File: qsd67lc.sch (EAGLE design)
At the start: 21 parts, among them IC1 MEGA8-P

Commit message: changed supply from 5V to 3V3
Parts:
- added JP1, JP2, JP3: (no value), pinhead:PINHD-1X3
- added U1: HC_05, Bluetooth HC-05:HC_05
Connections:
- net RXD_5V renamed RXD
- net TXD_5V renamed TXD
- removed net +5V: IC1.AREF, IC1.AVCC, IC1.VCC@1, R1.2, SV1.5
- removed net DLE: R2.2, R3.2, R4.2, R5.2, R6.2
- new net +3V3: IC1.AREF, IC1.AVCC, IC1.VCC@1, R1.2, R2.2, R3.2, R4.2, R5.2, R6.2
- new net MISO_EXT: JP2.1
- new net MISO_ISP: JP2.3, SV1.6
- new net MOSI_EXT: JP1.1
- new net MOSI_ISP: JP1.3, SV1.3
- new net SCK_EXT: JP3.1
- new net SCK_ISP: JP3.3, SV1.4
- net MISO: now also JP2.2; no longer SV1.6
- net MOSI: now also JP1.2; no longer SV1.3
- net SCK: now also JP3.2; no longer SV1.4
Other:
- note added: "jumper to detach other SPI devices while programming"

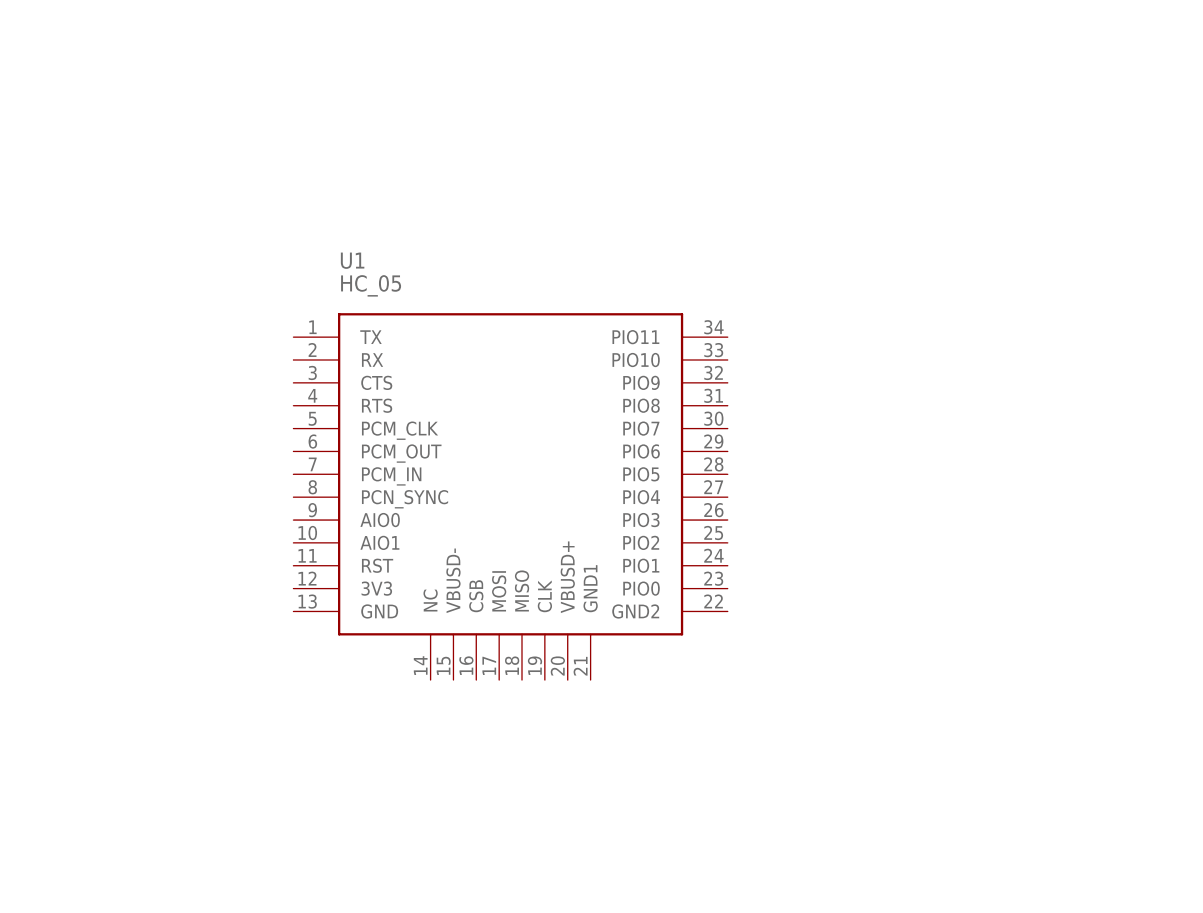
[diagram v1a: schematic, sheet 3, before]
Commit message: added hc05 circuits
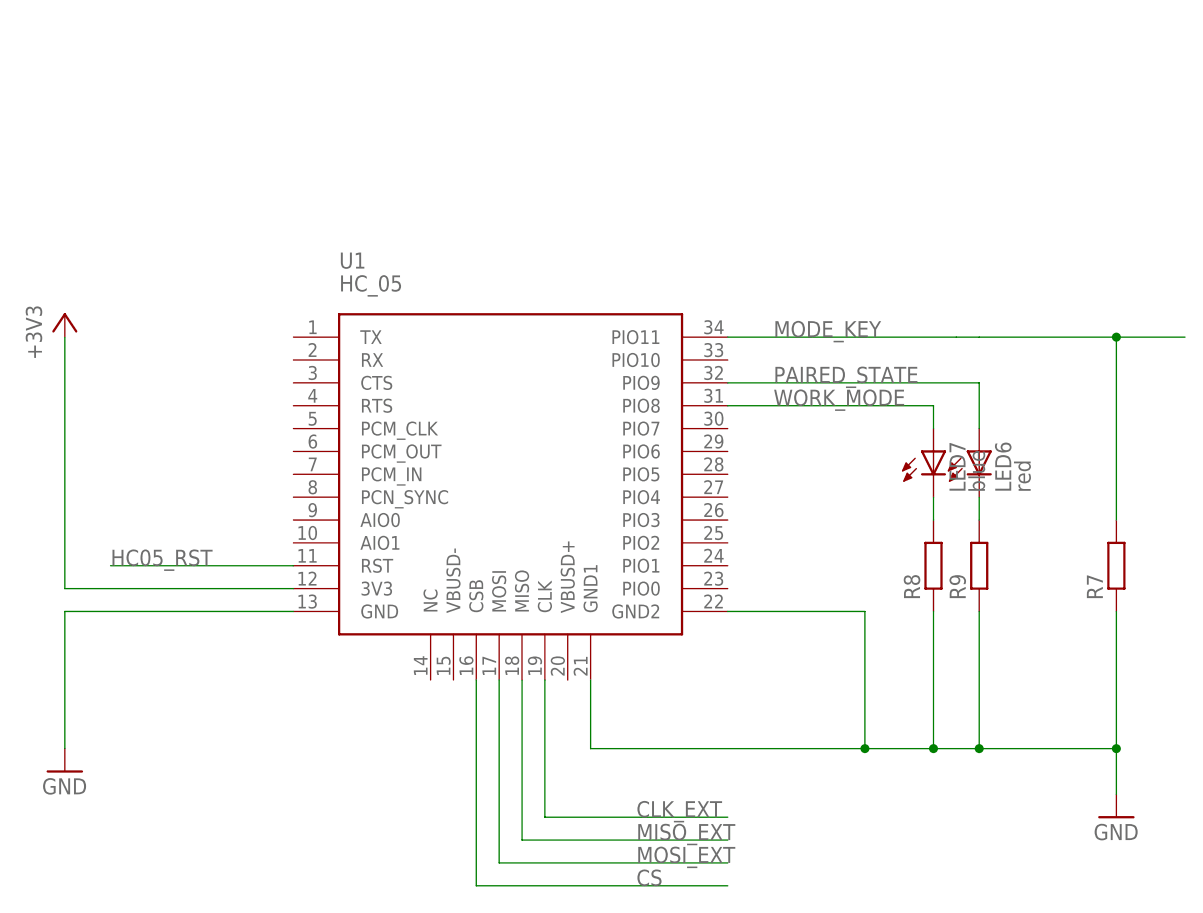
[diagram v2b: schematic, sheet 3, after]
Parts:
- added LED6: red, led:LEDCHIP-LED0805
- added LED7: blue, led:LEDCHIP-LED0805
- added R7, R8, R9: (no value), rcl:R-EU_R0805
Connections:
- new net CLK_EXT: U1.CLK
- new net CS: IC1.PB2(SS/OC1B), U1.CSB
- new net HC05_RST: IC1.PB0(ICP), U1.RST
- new net MODE_KEY: R7.2, U1.PIO11
- new net N$13: LED7.C, R8.2
- new net N$14: LED6.C, R9.2
- new net PAIRED_STATE: LED6.A, U1.PIO9
- new net WORK_MODE: LED7.A, U1.PIO8
- net +3V3: now also U1.3V3
- net GND: now also R7.1, R8.1, R9.1, U1.GND, U1.GND1, U1.GND2
- net MISO_EXT: now also U1.MISO
- net MOSI_EXT: now also U1.MOSI
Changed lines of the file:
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@@
 <part name="JP2" library="pinhead" library_urn="urn:adsk.eagle:library:325" deviceset="PINHD-1X3" device="" package3d_urn="urn:adsk.eagle:package:22458/2"/>
 <part name="JP3" library="pinhead" library_urn="urn:adsk.eagle:library:325" deviceset="PINHD-1X3" device="" package3d_urn="urn:adsk.eagle:package:22458/2"/>
+<part name="+3V1" library="hcontrol" deviceset="+3V3" device=""/>
+<part name="GND3" library="SparkFun-Aesthetics" deviceset="GND" device=""/>
+<part name="LED6" library="led" library_urn="urn:adsk.eagle:library:259" deviceset="LED" device="CHIP-LED0805" package3d_urn="urn:adsk.eagle:package:15818/2" value="red"/>
+<part name="LED7" library="led" library_urn="urn:adsk.eagle:library:259" deviceset="LED" device="CHIP-LED0805" package3d_urn="urn:adsk.eagle:package:15818/2" value="blue"/>
+<part name="R7" library="rcl" library_urn="urn:adsk.eagle:library:334" deviceset="R-EU_" device="R0805" package3d_urn="urn:adsk.eagle:package:23553/2"/>
+<part name="R8" library="rcl" library_urn="urn:adsk.eagle:library:334" deviceset="R-EU_" device="R0805" package3d_urn="urn:adsk.eagle:package:23553/2"/>
+<part name="R9" library="rcl" library_urn="urn:adsk.eagle:library:334" deviceset="R-EU_" device="R0805" package3d_urn="urn:adsk.eagle:package:23553/2"/>
+<part name="GND4" library="SparkFun-Aesthetics" deviceset="GND" device=""/>
 </parts>
 <sheets>
@@
 </segment>
 </net>
+<net name="CS" class="0">
+<segment>
+<pinref part="IC1" gate="G$1" pin="PB2(SS/OC1B)"/>
+<wire x1="22.86" y1="-20.32" x2="43.18" y2="-20.32" width="0.1524" layer="91"/>
+<label x="40.64" y="-20.32" size="1.778" layer="95"/>
+</segment>
+</net>
+<net name="HC05_RST" class="0">
+<segment>
+<pinref part="IC1" gate="G$1" pin="PB0(ICP)"/>
+<wire x1="22.86" y1="-15.24" x2="43.18" y2="-15.24" width="0.1524" layer="91"/>
+<label x="30.48" y="-15.24" size="1.778" layer="95"/>
+</segment>
+</net>
 </nets>
 </sheet>
@@
 <instances>
 <instance part="U1" gate="G$1" x="0" y="0"/>
+<instance part="+3V1" gate="G$1" x="-48.26" y="17.78"/>
+<instance part="GND3" gate="1" x="-48.26" y="-33.02"/>
+<instance part="LED6" gate="G$1" x="53.34" y="2.54"/>
+<instance part="LED7" gate="G$1" x="48.26" y="2.54"/>
+<instance part="R7" gate="G$1" x="68.58" y="-10.16" rot="R90"/>
+<instance part="R8" gate="G$1" x="48.26" y="-10.16" rot="R90"/>
+<instance part="R9" gate="G$1" x="53.34" y="-10.16" rot="R90"/>
+<instance part="GND4" gate="1" x="68.58" y="-38.1"/>
 </instances>
 <busses>
 </busses>
 <nets>
+<net name="+3V3" class="0">
+<segment>
+<pinref part="+3V1" gate="G$1" pin="+3V3"/>
+<pinref part="U1" gate="G$1" pin="3V3"/>
+<wire x1="-48.26" y1="15.24" x2="-48.26" y2="-12.7" width="0.1524" layer="91"/>
+<wire x1="-48.26" y1="-12.7" x2="-22.86" y2="-12.7" width="0.1524" layer="91"/>
+</segment>
+</net>
+<net name="GND" class="0">
+<segment>
+<pinref part="U1" gate="G$1" pin="GND"/>
+<pinref part="GND3" gate="1" pin="GND"/>
+<wire x1="-22.86" y1="-15.24" x2="-48.26" y2="-15.24" width="0.1524" layer="91"/>
+<wire x1="-48.26" y1="-15.24" x2="-48.26" y2="-30.48" width="0.1524" layer="91"/>
+</segment>
+<segment>
+<pinref part="R7" gate="G$1" pin="1"/>
+<pinref part="GND4" gate="1" pin="GND"/>
+<wire x1="68.58" y1="-15.24" x2="68.58" y2="-30.48" width="0.1524" layer="91"/>
+<pinref part="R9" gate="G$1" pin="1"/>
+<wire x1="68.58" y1="-30.48" x2="68.58" y2="-35.56" width="0.1524" layer="91"/>
+<wire x1="53.34" y1="-15.24" x2="53.34" y2="-30.48" width="0.1524" layer="91"/>
+<wire x1="53.34" y1="-30.48" x2="68.58" y2="-30.48" width="0.1524" layer="91"/>
+<junction x="68.58" y="-30.48"/>
+<pinref part="R8" gate="G$1" pin="1"/>
+<wire x1="48.26" y1="-15.24" x2="48.26" y2="-30.48" width="0.1524" layer="91"/>
+<wire x1="48.26" y1="-30.48" x2="53.34" y2="-30.48" width="0.1524" layer="91"/>
+<junction x="53.34" y="-30.48"/>
+<pinref part="U1" gate="G$1" pin="GND2"/>
+<wire x1="25.4" y1="-15.24" x2="40.64" y2="-15.24" width="0.1524" layer="91"/>
+<wire x1="40.64" y1="-15.24" x2="40.64" y2="-30.48" width="0.1524" layer="91"/>
+<wire x1="40.64" y1="-30.48" x2="48.26" y2="-30.48" width="0.1524" layer="91"/>
+<junction x="48.26" y="-30.48"/>
+<pinref part="U1" gate="G$1" pin="GND1"/>
+<wire x1="10.16" y1="-22.86" x2="10.16" y2="-30.48" width="0.1524" layer="91"/>
+<wire x1="10.16" y1="-30.48" x2="40.64" y2="-30.48" width="0.1524" layer="91"/>
+<junction x="40.64" y="-30.48"/>
+</segment>
+</net>
+<net name="CLK_EXT" class="0">
+<segment>
+<pinref part="U1" gate="G$1" pin="CLK"/>
+<wire x1="5.08" y1="-22.86" x2="5.08" y2="-38.1" width="0.1524" layer="91"/>
+<wire x1="5.08" y1="-38.1" x2="25.4" y2="-38.1" width="0.1524" layer="91"/>
+<label x="15.24" y="-38.1" size="1.778" layer="95"/>
+</segment>
+</net>
+<net name="MISO_EXT" class="0">
+<segment>
+<pinref part="U1" gate="G$1" pin="MISO"/>
+<wire x1="2.54" y1="-22.86" x2="2.54" y2="-40.64" width="0.1524" layer="91"/>
+<wire x1="2.54" y1="-40.64" x2="25.4" y2="-40.64" width="0.1524" layer="91"/>
+<label x="15.24" y="-40.64" size="1.778" layer="95"/>
+</segment>
+</net>
+<net name="MOSI_EXT" class="0">
+<segment>
+<pinref part="U1" gate="G$1" pin="MOSI"/>
+<wire x1="0" y1="-22.86" x2="0" y2="-43.18" width="0.1524" layer="91"/>
+<wire x1="0" y1="-43.18" x2="25.4" y2="-43.18" width="0.1524" layer="91"/>
+<label x="15.24" y="-43.18" size="1.778" layer="95"/>
+</segment>
+</net>
+<net name="CS" class="0">
+<segment>
+<pinref part="U1" gate="G$1" pin="CSB"/>
+<wire x1="-2.54" y1="-22.86" x2="-2.54" y2="-45.72" width="0.1524" layer="91"/>
+<wire x1="-2.54" y1="-45.72" x2="25.4" y2="-45.72" width="0.1524" layer="91"/>
+<label x="15.24" y="-45.72" size="1.778" layer="95"/>
+</segment>
+</net>
+<net name="MODE_KEY" class="0">
+<segment>
+<pinref part="U1" gate="G$1" pin="PIO11"/>
+<wire x1="25.4" y1="15.24" x2="50.8" y2="15.24" width="0.1524" layer="91"/>
+<wire x1="50.8" y1="15.24" x2="53.34" y2="15.24" width="0.1524" layer="91"/>
+<label x="30.48" y="15.24" size="1.778" layer="95"/>
+<pinref part="R7" gate="G$1" pin="2"/>
+<wire x1="53.34" y1="15.24" x2="68.58" y2="15.24" width="0.1524" layer="91"/>
+<wire x1="68.58" y1="15.24" x2="68.58" y2="-5.08" width="0.1524" layer="91"/>
+<wire x1="68.58" y1="15.24" x2="76.2" y2="15.24" width="0.1524" layer="91"/>
+<junction x="68.58" y="15.24"/>
+</segment>
+</net>
+<net name="PAIRED_STATE" class="0">
+<segment>
+<pinref part="U1" gate="G$1" pin="PIO9"/>
+<pinref part="LED6" gate="G$1" pin="A"/>
+<wire x1="25.4" y1="10.16" x2="53.34" y2="10.16" width="0.1524" layer="91"/>
+<wire x1="53.34" y1="10.16" x2="53.34" y2="5.08" width="0.1524" layer="91"/>
+<label x="30.48" y="10.16" size="1.778" layer="95"/>
+</segment>
+</net>
+<net name="WORK_MODE" class="0">
+<segment>
+<pinref part="U1" gate="G$1" pin="PIO8"/>
+<pinref part="LED7" gate="G$1" pin="A"/>
+<wire x1="25.4" y1="7.62" x2="48.26" y2="7.62" width="0.1524" layer="91"/>
+<wire x1="48.26" y1="7.62" x2="48.26" y2="5.08" width="0.1524" layer="91"/>
+<label x="30.48" y="7.62" size="1.778" layer="95"/>
+</segment>
+</net>
+<net name="N$13" class="0">
+<segment>
+<pinref part="R8" gate="G$1" pin="2"/>
+<pinref part="LED7" gate="G$1" pin="C"/>
+<wire x1="48.26" y1="-5.08" x2="48.26" y2="-2.54" width="0.1524" layer="91"/>
+</segment>
+</net>
+<net name="N$14" class="0">
+<segment>
+<pinref part="LED6" gate="G$1" pin="C"/>
+<pinref part="R9" gate="G$1" pin="2"/>
+<wire x1="53.34" y1="-2.54" x2="53.34" y2="-5.08" width="0.1524" layer="91"/>
+</segment>
+</net>
+<net name="HC05_RST" class="0">
+<segment>
+<pinref part="U1" gate="G$1" pin="RST"/>
+<wire x1="-22.86" y1="-10.16" x2="-43.18" y2="-10.16" width="0.1524" layer="91"/>
+<label x="-43.18" y="-10.16" size="1.778" layer="95"/>
+</segment>
+</net>
 </nets>
 </sheet>

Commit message: removed OBDII interface added ignition power circuit
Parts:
- removed JP1, JP2, JP3: (no value), pinhead:PINHD-1X3
- added IC2: BTS555E3146, infineon:BTS555E3146
- added Q2: IRLZ44Z, transistor-power:IRLZ44Z
- added R10, R11: (no value), rcl:R-EU_R0805
- C1: value (none) -> 100n
- C3, C4: value (none) -> 15p
- LED1: value (none) -> blue
- LED2: value (none) -> green
- LED3: value (none) -> red
- R1, R7: value (none) -> 10k
- R2, R3, R4, R5, R6, R8, R9: value (none) -> 220
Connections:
- removed net CLK_EXT: U1.CLK
- removed net MISO_EXT: JP2.1, U1.MISO
- removed net MISO_ISP: JP2.3, SV1.6
- removed net MOSI_EXT: JP1.1, U1.MOSI
- removed net MOSI_ISP: JP1.3, SV1.3
- removed net N$11: R6.1, S2.S, S2.S1
- removed net SCK_EXT: JP3.1
- removed net SCK_ISP: JP3.3, SV1.4
- new net +12V: IC2.VBB
- new net IGN_CTL: IC1.PD7(AIN1), Q2.G, R11.2
- new net IGN_OUT: IC2.O1, IC2.O2
- new net RPM_INT: IC1.PD3(INT1)
- net +3V3: now also R10.2, S1.S, S1.S1, S2.S, S2.S1; no longer R5.2, R6.2
- net CS: no longer U1.CSB
- net GND: now also Q2.S, R11.1, R5.1, R6.1
- net MISO: now also SV1.6; no longer JP2.2
- net MOSI: now also SV1.3; no longer JP1.2
- net N$10: now also IC2.IN, Q2.D, R10.1; no longer IC1.PC4(ADC4/SDA), S1.P, S1.P1
- net N$12: now also R6.2, S1.P, S1.P1; no longer S2.P, S2.P1
- net N$8: now also IC1.PC4(ADC4/SDA), R5.2, S2.P, S2.P1; no longer R5.1, S1.S, S1.S1
- net SCK: now also SV1.4; no longer JP3.2
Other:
- note removed: "jumper to detach other SPI devices while programming"

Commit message: added rs232 for direct PC communication
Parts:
- added C2: 100n, rcl:C-EUC0805
- added C5, C6, C7, C8: (no value), rcl:CPOL-EUE2.5-6
- added IC3: MAX3232CPE, maxim:MAX3232CPE
- added JP1: UART_SELECTOR, pinhead:PINHD-2X3
- added X1: RS232, con-subd:F09HP
- R10, R11: value (none) -> 10k
- R5, R6: value 220 -> 10k
- SV1: value (none) -> ISP
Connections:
- new net N$11: C7.+, IC3G$1.V+
- new net N$15: C8.-, IC3G$1.V-
- new net N$17: C5.+, IC3G$1.C1+
- new net N$18: C6.+, IC3G$1.C2+
- new net N$19: C6.-, IC3G$1.C2-
- new net N$20: C5.-, IC3G$1.C1-
- new net RS232_RX: IC3G$1.T1OUT, X1.2
- new net RS232_TX: IC3G$1.R1IN, X1.3
- new net RXD_BT: JP1.1, U1.TX
- new net RXD_RS232: IC3G$1.R1OUT, JP1.5
- new net TXD_BT: JP1.2, U1.RX
- new net TXD_RS232: IC3G$1.T1IN, JP1.6
- net +3V3: now also C2.1, IC3P.VCC
- net GND: now also C2.2, C7.-, C8.+, IC3P.GND, X1.1, X1.5
- net RXD: now also JP1.3
- net TXD: now also JP1.4
